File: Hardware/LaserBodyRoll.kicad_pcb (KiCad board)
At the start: 2 copper layers, 100 x 32 mm, 87 parts, among them J2 FTSH-105-01-L-DV-K, J3 FTSH-105-01-L-DV-K, J4 Conn_01x08, Q1 Q_NPN_BCE, U1 TPS821XX, U10 VL53L0X, U2 LDK130-ADJ_SOT23_SOT353, U3 STM32F303RETx, U4 LMC6032, U5 ITS42K5D, U6 CYBLE-022001-00, U7 TJA1051T-3, U8 ICM-20602, U9 W25Qxx, Y1 8MHz, Y2 32.768

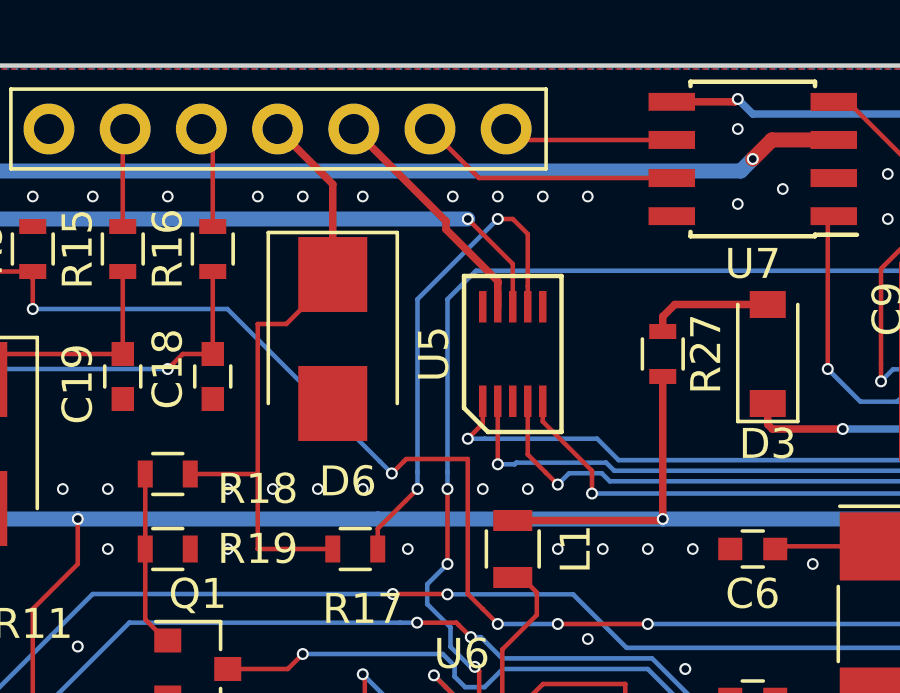
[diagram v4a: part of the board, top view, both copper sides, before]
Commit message: Added a resistor for the CAN phy lines. Added test points for SPI lines.
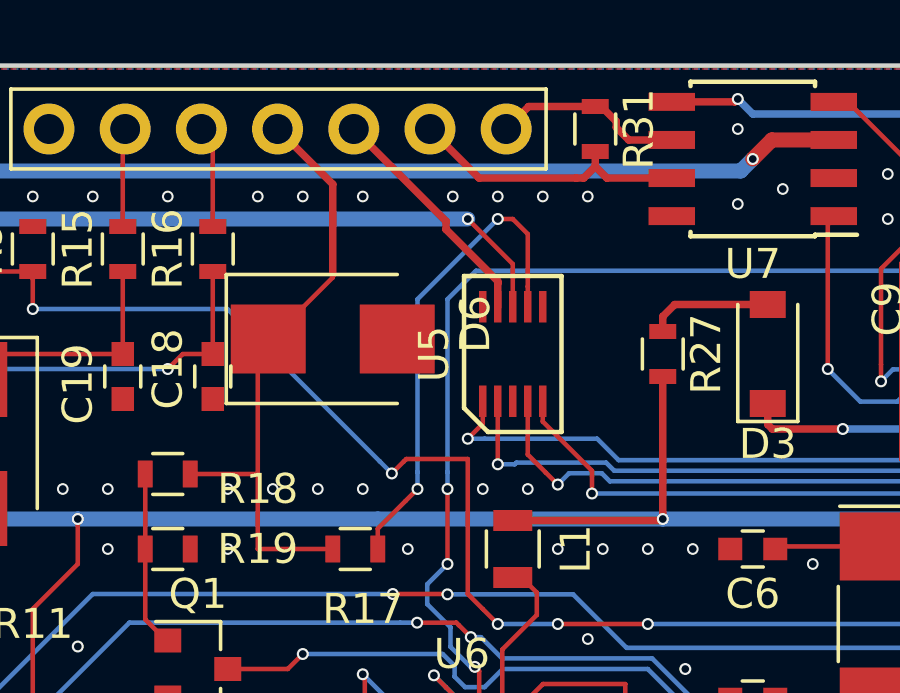
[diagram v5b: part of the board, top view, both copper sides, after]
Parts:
- added R31: 120, Resistors_SMD:R_0603, F.Cu at (68.8, 39.0)
- turned D6 to 0 degrees
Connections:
- J2 pad 6: /Processor/SWDV -> (no net)
- J2 pad 8: Net-(J2-Pad8) -> (no net)
- J3 pad 6: /Logic/SWDV -> (no net)
- J3 pad 8: Net-(J3-Pad8) -> (no net)
- U1 pad 7: Net-(U1-Pad7) -> (no net)
- U10 pad 8: Net-(U10-Pad8) -> (no net)
- U3 pad 15: Net-(U3-Pad15) -> (no net)
- U3 pad 16: Net-(U3-Pad16) -> (no net)
- U3 pad 2: Net-(U3-Pad2) -> (no net)
- U3 pad 24: Net-(U3-Pad24) -> (no net)
- U3 pad 26: Net-(U3-Pad26) -> (no net)
- U3 pad 37: Net-(U3-Pad37) -> (no net)
- U3 pad 38: Net-(U3-Pad38) -> (no net)
- U3 pad 39: Net-(U3-Pad39) -> (no net)
- U3 pad 42: Net-(U3-Pad42) -> (no net)
- U3 pad 43: Net-(U3-Pad43) -> (no net)
- U3 pad 53: Net-(U3-Pad53) -> (no net)
- U3 pad 54: Net-(U3-Pad54) -> (no net)
- U3 pad 56: Net-(U3-Pad56) -> (no net)
- U3 pad 58: Net-(U3-Pad58) -> (no net)
- U3 pad 59: Net-(U3-Pad59) -> (no net)
- U3 pad 61: Net-(U3-Pad61) -> (no net)
- U3 pad 62: Net-(U3-Pad62) -> (no net)
- U6 pad 15: Net-(U6-Pad15) -> (no net)
- U6 pad 16: Net-(U6-Pad16) -> (no net)
- U6 pad 17: Net-(U6-Pad17) -> (no net)
- U6 pad 20: Net-(U6-Pad20) -> (no net)
- U6 pad 21: Net-(U6-Pad21) -> (no net)
- U6 pad 8: Net-(U6-Pad8) -> (no net)
- U6 pad 9: Net-(U6-Pad9) -> (no net)
- U8 pad 7: Net-(U8-Pad7) -> (no net)
- U8 pad 8: Net-(U8-Pad8) -> (no net)
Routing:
- net CANL: track 5.67 -> 6.93 mm
- net CANH: track 8.74 -> 9.56 mm
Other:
- board text added: "AOUT1"
- board text added: "AOUT2"
- board text added: "CANH"
- board text added: "CANL"
- board text added: "DIN"
- board text added: "DOUT"
- board text added: "GND"
- board text added: "PWR"

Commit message: Routed test points
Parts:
- added TP10: , Connectors_TestPoints:Test_Point_Pad_d2.0mm, B.Cu at (88.8, 39.0)
- added TP11: , Connectors_TestPoints:Test_Point_Pad_d2.0mm, B.Cu at (80.8, 41.2)
- added TP12: , Connectors_TestPoints:Test_Point_Pad_d2.0mm, B.Cu at (121.8, 56.8)
- added TP13: , Connectors_TestPoints:Test_Point_Pad_d2.0mm, B.Cu at (95.0, 38.8)
- added TP14: , Connectors_TestPoints:Test_Point_Pad_d2.0mm, B.Cu at (120.0, 59.5)
- added TP15: , Connectors_TestPoints:Test_Point_Pad_d2.0mm, B.Cu at (83.5, 38.8)
- added TP16: , Connectors_TestPoints:Test_Point_Pad_d2.0mm, B.Cu at (116.2, 64.2)
- added TP5: , Connectors_TestPoints:Test_Point_Pad_d2.0mm, B.Cu at (96.0, 65.5)
- added TP6: , Connectors_TestPoints:Test_Point_Pad_d2.0mm, B.Cu at (92.8, 65.5)
- added TP7: , Connectors_TestPoints:Test_Point_Pad_d2.0mm, B.Cu at (87.5, 65.5)
- added TP8: , Connectors_TestPoints:Test_Point_Pad_d2.0mm, B.Cu at (70.0, 46.0)
- added TP9: , Connectors_TestPoints:Test_Point_Pad_d2.0mm, B.Cu at (115.2, 54.5)
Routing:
- net IMU_MISO: track 11.3 -> 22.7 mm
- net IMU_MOSI: track 12.2 -> 23.0 mm
- net FLASH_SCLK: track 25.0 -> 33.9 mm, vias 0 -> 1
- net FLASH_MOSI: track 19.3 -> 26.9 mm, vias 2 -> 3
- net IMU_CS: track 10.9 -> 17.8 mm, vias 0 -> 1
- net IMU_SCLK: track 11.2 -> 15.5 mm, vias 0 -> 1
- net BLE_MOSI: track 35.6 -> 39.5 mm
- net FLASH_CS: track 17.3 -> 20.6 mm
- net FLASH_MISO: track 17.9 -> 20.3 mm, vias 0 -> 1
- net BLE_SCLK: track 54.0 -> 56.3 mm
- net BLE_CS: track 61.2 -> 63.2 mm
- net BLE_MISO: track 35.1 -> 37.0 mm
- net CPU_DIN1: vias 3 -> 2

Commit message: Order this version of the board.
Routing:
- net 5V: track 82.5 -> 83.6 mm
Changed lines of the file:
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@@
     (thickness 1.6)
     (drawings 25)
-    (tracks 1047)
+    (tracks 1050)
     (zones 0)
     (modules 100)
@@
   )
   (setup
-    (last_trace_width 0.1524)
+    (last_trace_width 0.5)
     (user_trace_width 0.1524)
     (user_trace_width 0.5)
@@
     (tags "resistor 0603")
     (attr smd)
-    (fp_text reference R30 (at 0 -1.45) (layer F.SilkS)
+    (fp_text reference R30 (at 2.75 0) (layer F.SilkS)
       (effects (font (size 1 1) (thickness 0.15)))
     )
@@
     (tags "capacitor 0603")
     (attr smd)
-    (fp_text reference C22 (at -2.5 0) (layer F.SilkS)
+    (fp_text reference C22 (at -2.75 0) (layer F.SilkS)
       (effects (font (size 1 1) (thickness 0.15)))
     )
@@
     (tags "capacitor 0603")
     (attr smd)
-    (fp_text reference C21 (at 0 2) (layer F.SilkS)
+    (fp_text reference C21 (at 0 1.75) (layer F.SilkS)
       (effects (font (size 1 1) (thickness 0.15)))
     )
@@
     (tags "capacitor 0603")
     (attr smd)
-    (fp_text reference C9 (at 2.5 0 270) (layer F.SilkS)
+    (fp_text reference C9 (at 2.75 0) (layer F.SilkS)
       (effects (font (size 1 1) (thickness 0.15)))
     )
@@
     (tags "capacitor 0603")
     (attr smd)
-    (fp_text reference C12 (at 0 -2) (layer F.SilkS)
+    (fp_text reference C12 (at 0 2.25) (layer F.SilkS)
       (effects (font (size 1 1) (thickness 0.15)))
     )
@@
     (tags "capacitor 0603")
     (attr smd)
-    (fp_text reference C14 (at -0.5 -2.5 180) (layer F.SilkS)
+    (fp_text reference C14 (at -1.25 -2.25 180) (layer F.SilkS)
       (effects (font (size 1 1) (thickness 0.15)))
     )
@@
     (tags "resistor 0603")
     (attr smd)
-    (fp_text reference R5 (at 2.25 0 -90) (layer F.SilkS)
+    (fp_text reference R5 (at -2.5 0) (layer F.SilkS)
       (effects (font (size 1 1) (thickness 0.15)))
     )
@@
     (tags "resistor 0603")
     (attr smd)
-    (fp_text reference R6 (at 2.25 0 -90) (layer F.SilkS)
+    (fp_text reference R6 (at -2.5 0) (layer F.SilkS)
       (effects (font (size 1 1) (thickness 0.15)))
     )
@@
     (tags "resistor 0603")
     (attr smd)
-    (fp_text reference R21 (at 2.5 0) (layer F.SilkS)
+    (fp_text reference R21 (at 3 0) (layer F.SilkS)
       (effects (font (size 1 1) (thickness 0.15)))
     )
@@
     (tags "resistor 0603")
     (attr smd)
-    (fp_text reference R23 (at 1 2 180) (layer F.SilkS)
+    (fp_text reference R23 (at 0.5 2.5 180) (layer F.SilkS)
       (effects (font (size 1 1) (thickness 0.15)))
     )
@@
     (tags "CMS SM")
     (attr smd)
-    (fp_text reference C3 (at -2.222 -2 180) (layer F.SilkS)
+    (fp_text reference C3 (at -0.25 -3 180) (layer F.SilkS)
       (effects (font (size 1 1) (thickness 0.15)))
     )
@@
     (tags "capacitor 0603")
     (attr smd)
-    (fp_text reference C8 (at 2.5 0 90) (layer F.SilkS)
+    (fp_text reference C8 (at 2.75 0 180) (layer F.SilkS)
       (effects (font (size 1 1) (thickness 0.15)))
     )
@@
     (tags "capacitor 0603")
     (attr smd)
-    (fp_text reference C25 (at -3.5 0) (layer F.SilkS)
+    (fp_text reference C25 (at 0 1.25) (layer F.SilkS)
       (effects (font (size 1 1) (thickness 0.15)))
     )
@@
     (tags "Diode SMB (DO-214AA)")
     (attr smd)
-    (fp_text reference D4 (at -4.5 -0.5) (layer F.SilkS)
+    (fp_text reference D4 (at -2.25 3) (layer F.SilkS)
       (effects (font (size 1 1) (thickness 0.15)))
     )
@@
     (descr "Through hole straight pin header, 1x08, 2.54mm pitch, single row")
     (tags "Through hole pin header THT 1x08 2.54mm single row")
-    (fp_text reference J4 (at 0 -2.33 90) (layer F.SilkS)
+    (fp_text reference J4 (at 1 -2.75 180) (layer F.SilkS)
       (effects (font (size 1 1) (thickness 0.15)))
     )
@@
     (tags "CMS SOJ")
     (attr smd)
-    (fp_text reference U4 (at 0 -1.27) (layer F.SilkS)
+    (fp_text reference U4 (at 3.75 -1.5) (layer F.SilkS)
       (effects (font (size 1 1) (thickness 0.15)))
     )
@@
     (tags "SMD SMT crystal hand-soldering")
     (attr smd)
-    (fp_text reference Y2 (at 0 -1.95 180) (layer F.SilkS)
+    (fp_text reference Y2 (at -4 1 180) (layer F.SilkS)
       (effects (font (size 1 1) (thickness 0.15)))
     )
@@
   (segment (start 31 46) (end 31 48) (width 0.1524) (layer F.Cu) (net 9))
   (segment (start 29.75 46) (end 31 46) (width 0.1524) (layer F.Cu) (net 9))
+  (segment (start 33.05 60.35) (end 33.05 60) (width 0.5) (layer F.Cu) (net 10))
+  (segment (start 33.05 60) (end 33.05 59.45) (width 0.5) (layer F.Cu) (net 10))
+  (segment (start 30.25 60.5) (end 30.75 60) (width 0.5) (layer F.Cu) (net 10))
+  (segment (start 30.75 60) (end 33.05 60) (width 0.5) (layer F.Cu) (net 10))
+  (segment (start 30.25 61.75) (end 30.25 60.5) (width 0.5) (layer F.Cu) (net 10))
+  (segment (start 30.5 62) (end 30.25 61.75) (width 0.5) (layer F.Cu) (net 10))
+  (segment (start 31.875 62) (end 30.5 62) (width 0.5) (layer F.Cu) (net 10))
+  (segment (start 33.05 61.65) (end 32.225 61.65) (width 0.5) (layer F.Cu) (net 10))
+  (segment (start 32.225 61.65) (end 31.875 62) (width 0.5) (layer F.Cu) (net 10))
   (segment (start 37 43) (end 37 53.434315) (width 0.5) (layer B.Cu) (net 10))
   (segment (start 37 53.434315) (end 37 54) (width 0.5) (layer B.Cu) (net 10))
@@
   (segment (start 39.766 58) (end 39.766 56.766) (width 0.5) (layer F.Cu) (net 10))
   (segment (start 39.766 56.766) (end 37 54) (width 0.5) (layer F.Cu) (net 10))
-  (segment (start 33.05 60.35) (end 33.05 59.45) (width 0.5) (layer F.Cu) (net 10))
   (segment (start 33.05 59.45) (end 37 55.5) (width 0.5) (layer F.Cu) (net 10))
   (segment (start 37 55.5) (end 37 54) (width 0.5) (layer F.Cu) (net 10))
@@
   (segment (start 39.766 58) (end 42.091 60.325) (width 0.5) (layer F.Cu) (net 10))
   (segment (start 42.091 60.325) (end 42.595 60.325) (width 0.5) (layer F.Cu) (net 10))
-  (segment (start 30.5 61.5) (end 30.5 60.5) (width 0.5) (layer F.Cu) (net 10))
-  (segment (start 33.05 60.35) (end 30.65 60.35) (width 0.5) (layer F.Cu) (net 10))
-  (segment (start 30.65 60.35) (end 30.5 60.5) (width 0.5) (layer F.Cu) (net 10))
-  (segment (start 30.65 61.65) (end 30.5 61.5) (width 0.5) (layer F.Cu) (net 10))
-  (segment (start 33.05 61.65) (end 30.65 61.65) (width 0.5) (layer F.Cu) (net 10))
   (segment (start 34 52.95) (end 34.825 52.95) (width 0.5) (layer F.Cu) (net 10))
   (segment (start 34.825 52.95) (end 37 50.775) (width 0.5) (layer F.Cu) (net 10))

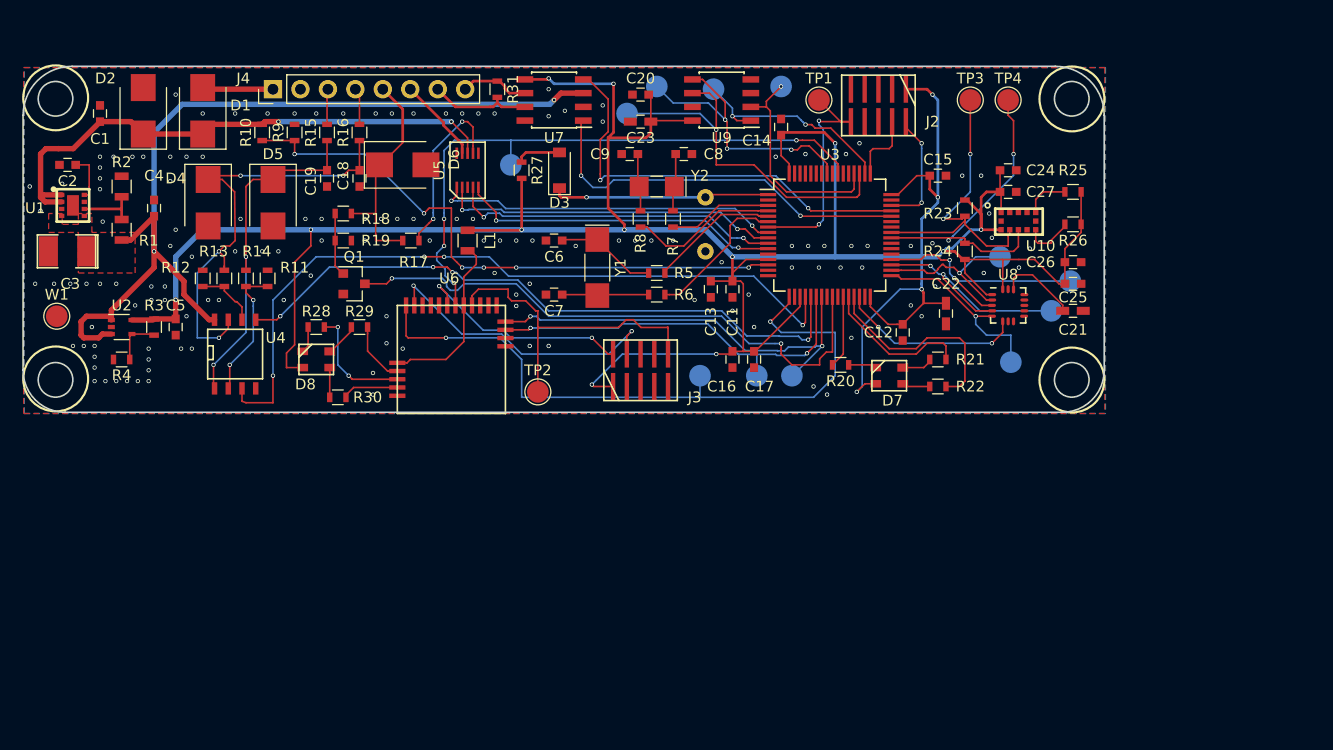
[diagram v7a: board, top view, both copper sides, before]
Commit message: Added some libraries and mechanical drawings for the box.
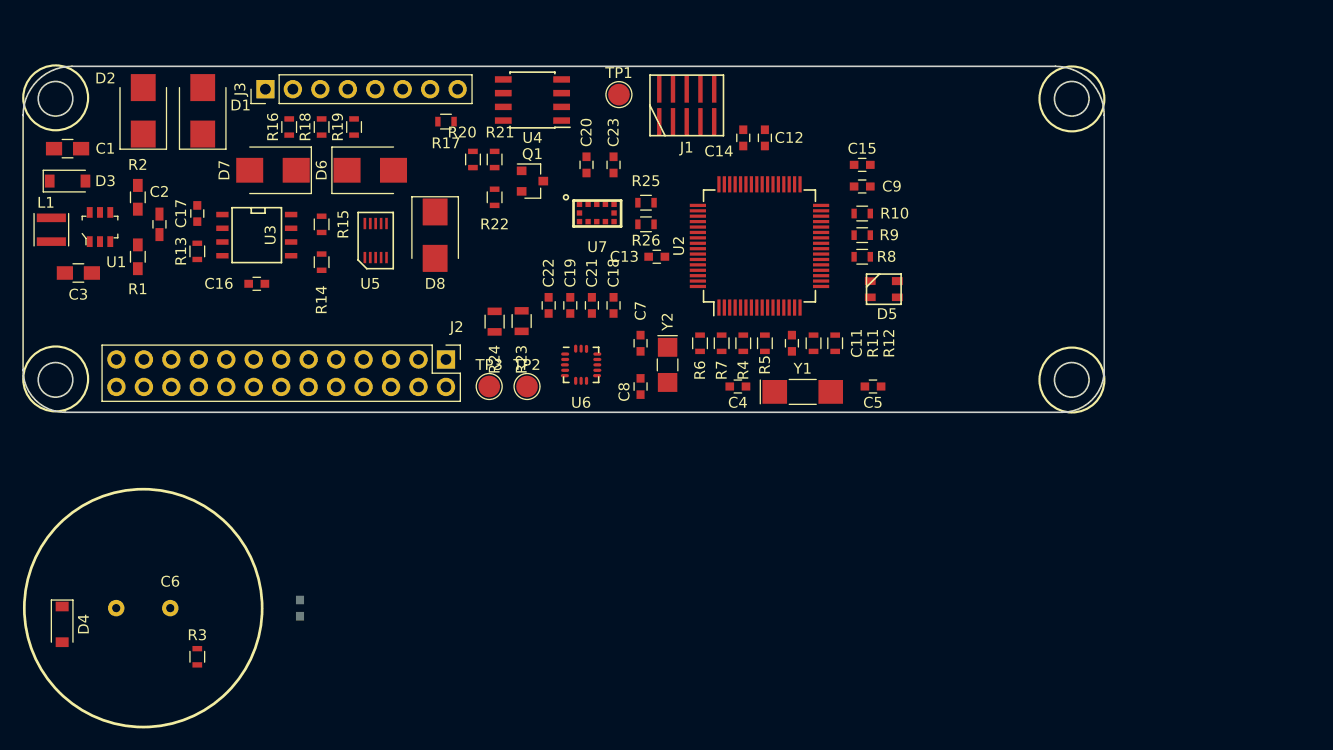
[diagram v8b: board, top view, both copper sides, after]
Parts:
- removed C24: 0.1u, Capacitors_SMD:C_0603
- removed C25: 2.2U, Capacitors_SMD:C_0603
- removed C26: 10n, Capacitors_SMD:C_0603
- removed C27: 4.7u, Capacitors_SMD:C_0603
- removed J4: Conn_01x08, Pin_Headers:Pin_Header_Straight_1x08_Pitch2.54mm
- removed R27: 25, Resistors_SMD:R_0603
- removed R28, R29, R30: 330, Resistors_SMD:R_0603
- removed R31: 120, Resistors_SMD:R_0603
- removed TP10, TP11, TP12, TP13, TP14, TP15, TP16, TP5, TP6, TP7, TP8, TP9: , Connectors_TestPoints:Test_Point_Pad_d2.0mm
- removed TP4: Test_Point, Connectors_TestPoints:Test_Point_Pad_d2.0mm
- removed U10: VL53L0X, KicadFootprint:VL53L0x
- removed U8: ICM-20602, KicadFootprint:QFN-16-no_center_3x3mm_Pitch0.5mm
- removed U9: W25Qxx, Housings_SOIC:SOIC-8_3.9x4.9mm_Pitch1.27mm
- removed W1: TEST_1P, Connectors_TestPoints:Test_Point_Pad_d2.0mm
- added J1: FTSH-105-01-L-DV-K, KicadFootprint:FTSH-105-01-L-DV-K, F.Cu at (86.3, 40.5)
- C1: footprint Capacitors_SMD:C_0603 -> Capacitors_SMD:C_0805_HandSoldering
- C10: value 1.5F -> 100n; footprint KicadFootprint:Elna_Dynacap -> Capacitors_SMD:C_0603
- C11: value 4.7u -> 100n
- C14: value 100n -> 1u
- C15: value 100n -> 10n
- C16: value 1u -> 10n
- C18, C19: value 10n -> 0.1u
- C2: value 3.3n -> 10n; footprint Capacitors_SMD:C_0603 -> Capacitors_SMD:C_0603_HandSoldering
- C20: value 0.1n -> 0.1u
- C21: value 0.1u -> 2.2U; footprint Capacitors_SMD:C_0603_HandSoldering -> Capacitors_SMD:C_0603
- C22: value 0.1u -> 10n; footprint Capacitors_SMD:C_0603_HandSoldering -> Capacitors_SMD:C_0603
- C23: value 1u -> 4.7u; footprint Capacitors_SMD:C_0603_HandSoldering -> Capacitors_SMD:C_0603
- C3: value 22u -> 10u; footprint SMD_Packages:SMD-1210_Pol -> Capacitors_SMD:C_0805_HandSoldering
- C4: value 1u -> 20p
- C5: value 2.2U -> 20p
- C6: value 20p -> 1.5F; footprint Capacitors_SMD:C_0603 -> KicadFootprint:Elna_Dynacap
- C7: value 20p -> 6.8p
- C8: value 6.8 -> 6.8p
- C9: value 6.8 -> 4.7u
- D3: value D -> D_Schottky
- D4: value D_Zener -> D; footprint Diodes_SMD:D_SMB -> Diodes_SMD:D_SOD-123
- D5: value D_Zener -> CLV1L-FKB; footprint Diodes_SMD:D_SMB -> KicadFootprint:CREE_PLCC4
- D6: value D_TVS -> D_Zener
- D7: value LED_RABG -> D_Zener; footprint KicadFootprint:CREE_PLCC4 -> Diodes_SMD:D_SMB
- D8: value LED_RABG -> D_TVS; footprint KicadFootprint:CREE_PLCC4 -> Diodes_SMD:D_SMB
- J2: value FTSH-105-01-L-DV-K -> Conn_02x13_Odd_Even; footprint KicadFootprint:FTSH-105-01-L-DV-K -> Pin_Headers:Pin_Header_Straight_2x13_Pitch2.54mm
- J3: value FTSH-105-01-L-DV-K -> Conn_01x08; footprint KicadFootprint:FTSH-105-01-L-DV-K -> Pin_Headers:Pin_Header_Straight_1x08_Pitch2.54mm
- L1: value L_Core_Ferrite -> 4.7u; footprint Inductors_SMD:L_0805 -> Inductors_SMD:L_Taiyo-Yuden_MD-3030
- R1: value 525k -> 49.9k; footprint Resistors_SMD:R_0805 -> Resistors_SMD:R_0603_HandSoldering
- R10: value 75k -> 330
- R11: value 24.3k -> 10k
- R12: value 24.3k -> 75k
- R13, R14: value 24.3k -> 44.2k
- R17: value 24.3k -> 120
- R2: value 100k -> 9.53k; footprint Resistors_SMD:R_0805 -> Resistors_SMD:R_0603_HandSoldering
- R20, R21, R22: value 330 -> 24.3k
- R23, R24: footprint Resistors_SMD:R_0603 -> Resistors_SMD:R_0805
- R3: value 360 -> 25
- R4: value 120 -> 0
- R8: value 0 -> 330
- R9: value 10k -> 330
- U1: value TPS821XX -> AOZ1280CI; footprint KicadFootprint:TPS821XX -> digikey-footprints:SOT-23-6
- U2: value LDK130-ADJ_SOT23_SOT353 -> STM32F303RETx; footprint TO_SOT_Packages_SMD:SOT-353_SC-70-5 -> Housings_QFP:TQFP-64_10x10mm_Pitch0.5mm
- U3: value STM32F303RETx -> LMC6032; footprint Housings_QFP:TQFP-64_10x10mm_Pitch0.5mm -> SMD_Packages:SOIC-8-N
- U4: value LMC6032 -> TJA1051T-3; footprint SMD_Packages:SOIC-8-N -> Housings_SOIC:SOIC-8_3.9x4.9mm_Pitch1.27mm
- U6: value CYBLE-022001-00 -> ICM-20602; footprint KicadFootprint:CYBLE-022001 -> KicadFootprint:QFN-16-no_center_3x3mm_Pitch0.5mm
- U7: value TJA1051T-3 -> VL53L0X; footprint Housings_SOIC:SOIC-8_3.9x4.9mm_Pitch1.27mm -> KicadFootprint:VL53L0x
- moved C5 64.7 mm to (103.5, 66.5), turned to 0 degrees
- moved D7 60.1 mm to (48.0, 46.5), turned to 180 degrees
- moved U2 59.5 mm to (93.0, 53.5), turned to 90 degrees
- moved R12 58.8 mm to (100.0, 62.5)
- moved R4 57.5 mm to (91.5, 62.5), turned to 270 degrees
- moved D5 57.1 mm to (104.5, 57.5), turned to 0 degrees
- moved C4 56.5 mm to (91.0, 66.5), turned to 180 degrees
- moved R10 56.0 mm to (102.5, 50.5), turned to 180 degrees
- moved C10 53.4 mm to (50.5, 87.0)
- moved R9 53.4 mm to (102.5, 52.5), turned to 180 degrees
- moved C17 53.2 mm to (41.0, 50.5)
- moved U3 53.0 mm to (46.5, 52.5), turned to 270 degrees
- moved TP3 51.8 mm to (68.0, 66.5)
- moved R11 50.9 mm to (98.0, 62.5)
- moved C6 49.2 mm to (38.5, 87.0)
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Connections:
- C10 pad 1: Net-(C10-Pad1) -> VCC
- C16 pad 1: VCC -> Net-(C16-Pad1)
- C17 pad 1: VCC -> Net-(C17-Pad1)
- C19 pad 1: Net-(C19-Pad1) -> VCC
- C2 pad 2: GND -> Net-(C2-Pad2)
- C21 pad 1: Net-(C21-Pad1) -> VCC
- C4 pad 1: 5V -> Net-(C4-Pad1)
- C5 pad 1: VCC -> Net-(C5-Pad1)
- C9 pad 1: Net-(C9-Pad1) -> VCC
- D1 pad 2: PWR_IN -> VIN
- D3 pad 1: Net-(C10-Pad1) -> Net-(C2-Pad1)
- D3 pad 2: Net-(D3-Pad2) -> GND
- D4 pad 1: Net-(C18-Pad1) -> Net-(C6-Pad1)
- D4 pad 2: GND -> Net-(D4-Pad2)
- D5 pad 1: Net-(C19-Pad1) -> VCC
- D5 pad 2: GND -> Net-(D5-Pad2)
- D6 pad 1: /IO/DIN -> Net-(C16-Pad1)
- D7 pad 1: Net-(D7-Pad1) -> Net-(C17-Pad1)
- D7 pad 2: VCC -> GND
- D8 pad 1: Net-(D8-Pad1) -> /IO/DIN
- D8 pad 2: VCC -> GND
- J2 pad 10: /Processor/STM_RES -> (no net)
- J2 pad 2: /Processor/STM_SWDIO -> 5V
- J2 pad 3: GND -> SDA
- J2 pad 4: /Processor/STM_SWDCLK -> 5V
- J2 pad 5: GND -> SCL
- J2 pad 6: (no net) -> GND
- J2 pad 7: GND -> (no net)
- J3 pad 1: VCC -> VIN
- J3 pad 2: /Logic/SWDIO -> GND
- J3 pad 3: GND -> /IO/ANA_OUT1
- J3 pad 4: /Logic/SWDCLK -> /IO/ANA_OUT2
- J3 pad 5: GND -> /IO/DOUT
- J3 pad 6: (no net) -> /IO/DIN
- J3 pad 7: GND -> /IO/CANH
- J3 pad 8: (no net) -> /IO/CANL
- L1 pad 1: VCC -> Net-(C2-Pad1)
- L1 pad 2: Net-(L1-Pad2) -> 5V
- R10 pad 1: 12V -> Net-(D5-Pad4)
- R11 pad 1: Net-(R11-Pad1) -> GND
- R11 pad 2: GND -> Net-(R11-Pad2)
- R12 pad 1: Net-(R12-Pad1) -> 12V
- R12 pad 2: GND -> Net-(R11-Pad2)
- R13 pad 1: Net-(R12-Pad1) -> Net-(R13-Pad1)
- R13 pad 2: Net-(C18-Pad1) -> GND
- R14 pad 1: Net-(R11-Pad1) -> Net-(R14-Pad1)
- R14 pad 2: Net-(C19-Pad1) -> GND
- R15 pad 1: /IO/ANA_OUT1 -> Net-(R14-Pad1)
- R15 pad 2: Net-(C19-Pad1) -> Net-(C16-Pad1)
- R16 pad 1: /IO/ANA_OUT2 -> Net-(R13-Pad1)
- R16 pad 2: Net-(C18-Pad1) -> Net-(C17-Pad1)
- R17 pad 1: /IO/DIN -> /IO/CANL
- R17 pad 2: /IO/12V_PULLUP -> /IO/CANH
- R18 pad 1: /IO/DIN -> /IO/ANA_OUT1
- R18 pad 2: Net-(Q1-Pad1) -> Net-(C17-Pad1)
- R19 pad 1: Net-(Q1-Pad1) -> /IO/ANA_OUT2
- R19 pad 2: GND -> Net-(C16-Pad1)
- R20 pad 1: Net-(D7-Pad1) -> /IO/DIN
- R20 pad 2: RED -> /IO/12V_PULLUP
- R21 pad 1: Net-(D7-Pad4) -> /IO/DIN
- R21 pad 2: GREEN -> Net-(Q1-Pad1)
- R22 pad 1: Net-(D7-Pad3) -> Net-(Q1-Pad1)
- R22 pad 2: BLUE -> GND
- R23 pad 1: VCC -> Net-(R23-Pad1)
- R24 pad 1: VCC -> Net-(R23-Pad1)
- R25 pad 1: VCC -> Net-(R25-Pad1)
- R26 pad 1: VCC -> Net-(R25-Pad1)
- R3 pad 1: VCC -> Net-(D4-Pad2)
- R3 pad 2: Net-(R3-Pad2) -> VCC
- R4 pad 1: Net-(R3-Pad2) -> Net-(R4-Pad1)
- R4 pad 2: GND -> Net-(C4-Pad1)
- R5 pad 2: Net-(C6-Pad1) -> Net-(C5-Pad1)
- R8 pad 1: Net-(R8-Pad1) -> Net-(D5-Pad2)
- R8 pad 2: Net-(C9-Pad1) -> Net-(R8-Pad2)
- R9 pad 1: GND -> Net-(D5-Pad3)
- R9 pad 2: Net-(R10-Pad2) -> Net-(R9-Pad2)
- TP2 pad 1: /Logic/XRES -> SCL
- TP3 pad 1: SCL -> SDA
- U1 pad 1: 12V -> Net-(C2-Pad2)
- U1 pad 2: 12V -> GND
- U1 pad 3: GND -> Net-(R1-Pad2)
- U1 pad 4: 5V -> 12V
- U1 pad 5: 5V -> 12V
- U1 pad 6: Net-(R1-Pad2) -> Net-(C2-Pad1)
- U2 pad 1: 5V -> Net-(C6-Pad1)
- U2 pad 2: GND -> (no net)
- U2 pad 3: 5V -> Net-(R6-Pad1)
- U2 pad 4: Net-(R3-Pad2) -> Net-(R7-Pad1)
- U2 pad 5: VCC -> Net-(R4-Pad1)
- U3 pad 1: Net-(C10-Pad1) -> Net-(C17-Pad1)
- U3 pad 2: (no net) -> Net-(R13-Pad1)
- U3 pad 3: Net-(R7-Pad1) -> DAC1
- U3 pad 4: Net-(R8-Pad1) -> GND
- U3 pad 5: Net-(R5-Pad1) -> DAC2
- U3 pad 6: Net-(R6-Pad1) -> Net-(R14-Pad1)
- U3 pad 7: /Processor/STM_RES -> Net-(C16-Pad1)
- U3 pad 8: CPU_DOUT1 -> 5V
- U4 pad 1: Net-(C19-Pad1) -> CAN_TXD
- U4 pad 2: Net-(R11-Pad1) -> GND
- U4 pad 3: DAC1 -> 5V
- U4 pad 4: GND -> CAN_RXD
- U4 pad 5: DAC2 -> VCC
- U4 pad 6: Net-(R12-Pad1) -> /IO/CANL
- U4 pad 7: Net-(C18-Pad1) -> /IO/CANH
- U4 pad 8: 5V -> GND
- U6 pad 1: GND -> VCC
- U6 pad 11: /Logic/SWDIO -> GND
- U6 pad 12: BLE_SCLK -> GND
- U6 pad 13: Net-(L1-Pad2) -> GND
- U6 pad 14: /Logic/XRES -> Net-(C18-Pad1)
- U6 pad 15: (no net) -> GND
- U6 pad 16: (no net) -> VCC
- U6 pad 2: Net-(R30-Pad2) -> SCL
- U6 pad 3: Net-(R28-Pad2) -> SDA
- U6 pad 4: Net-(R29-Pad2) -> GND
- U6 pad 5: Net-(L1-Pad2) -> VCC
- U6 pad 6: BLE_CS -> IMU_INT
- U6 pad 7: /Logic/SWDCLK -> (no net)
- U6 pad 9: (no net) -> GND
- U7 pad 1: CAN_TXD -> VCC
- U7 pad 3: 5V -> GND
- U7 pad 4: CAN_RXD -> GND
- U7 pad 5: VCC -> /Logic/VL53L0X_XSHUT
- U7 pad 6: CANL -> GND
- U7 pad 7: CANH -> /Logic/VL53L0X_GP
- U7 pad 8: GND -> (no net)
- Y1 pad 1: Net-(C6-Pad1) -> Net-(C4-Pad1)
- Y1 pad 2: Net-(C7-Pad1) -> Net-(C5-Pad1)
- Y2 pad 1: Net-(C8-Pad1) -> Net-(C7-Pad1)
- Y2 pad 2: Net-(C9-Pad1) -> Net-(C8-Pad1)
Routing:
- net VCC: track 305.7 -> 0.00 mm, vias 16 -> 0
- net 5V: track 83.6 -> 0.00 mm, vias 2 -> 0
- net DAC1: track 69.6 -> 0.00 mm, vias 4 -> 0
- net BLE_CS: track 63.2 -> 0.00 mm, vias 2 -> 0
- net DAC2: track 60.0 -> 0.00 mm, vias 4 -> 0
- net BLE_SCLK: track 56.3 -> 0.00 mm, vias 4 -> 0
- net Net-(R10-Pad2): track 55.5 -> 0.00 mm, vias 6 -> 0
- net CPU_DIN1: track 54.0 -> 0.00 mm, vias 2 -> 0
- net 12V: track 51.9 -> 0.00 mm, vias 2 -> 0
- net Net-(C18-Pad1): track 41.7 -> 0.00 mm, vias 4 -> 0
- net BLE_MOSI: track 39.5 -> 0.00 mm, vias 2 -> 0
- net CAN_RXD: track 39.3 -> 0.00 mm, vias 2 -> 0
- net BLE_MISO: track 37.0 -> 0.00 mm, vias 2 -> 0
- net CAN_TXD: track 36.0 -> 0.00 mm, vias 2 -> 0
- net FLASH_SCLK: track 33.9 -> 0.00 mm, vias 1 -> 0
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- removed copper zone on F.Cu, net 5V
- removed copper zone on B.Cu, net GND
- removed copper zone on F.Cu, net GND
